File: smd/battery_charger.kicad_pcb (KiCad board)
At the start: 2 copper layers, 18.8 x 9.4 mm, 8 parts, among them J1 USB_OTG, U1 MCP73831

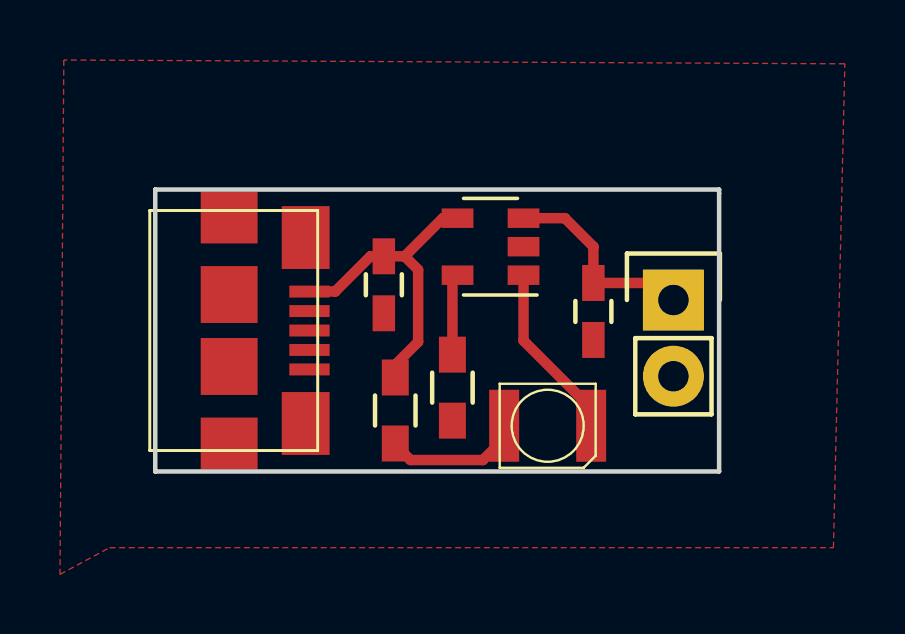
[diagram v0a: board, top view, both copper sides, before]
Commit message: Made the board almost half as big as before
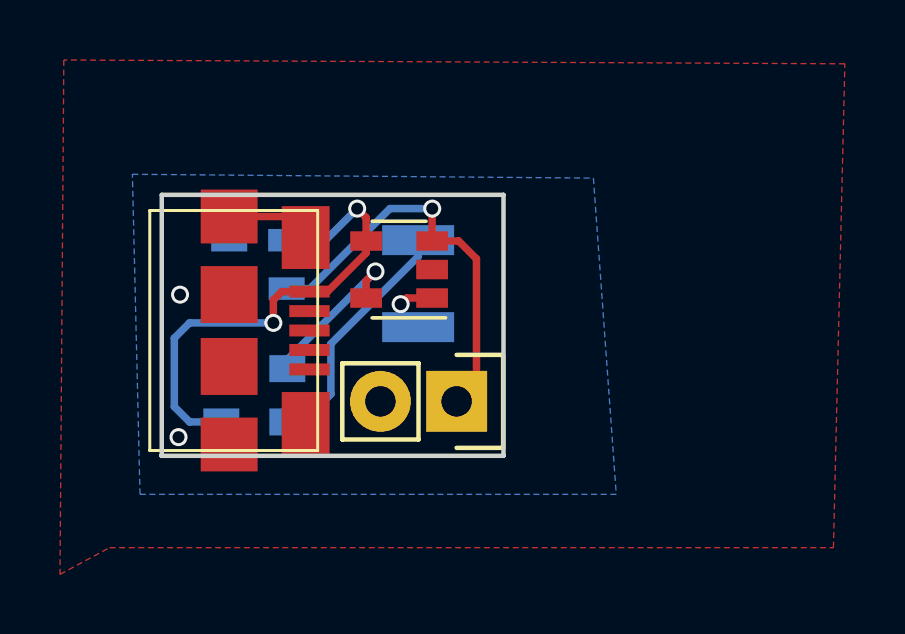
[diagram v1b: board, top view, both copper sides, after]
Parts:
- C1, C2, D1, R1, R2: moved to B.Cu
- moved C2 11.2 mm to (139.2, 104.0), turned to 180 degrees
- moved BT1 7.98 mm to (145.8, 107.7), turned to 180 degrees
- moved R2 6.63 mm to (139.1, 106.6), turned to 0 degrees
- moved D1 6.41 mm to (144.5, 103.8), turned to 180 degrees
- moved R1 4.71 mm to (139.1, 108.4), turned to 0 degrees
- moved C1 4.46 mm to (139.2, 102.3), turned to 0 degrees
- moved U1 3.14 mm to (143.9, 103.3)
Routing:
- net Net-(BT1-Pad1): track 6.83 -> 13.8 mm, vias 0 -> 1
- net +5V: track 10.4 -> 16.5 mm, vias 0 -> 2
- net Net-(D1-Pad1): track 5.95 -> 2.21 mm, vias 0 -> 1
- net Net-(D1-Pad2): track 4.61 -> 8.17 mm
- net GNDREF: track 0.00 -> 2.84 mm, vias 0 -> 2
- net Net-(R2-Pad2): track 2.72 -> 5.48 mm, vias 0 -> 1
- added copper zone on B.Cu, net GNDREF
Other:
- board size 18.8 x 9.4 mm -> 11.4 x 8.7 mm
- net class Default: trace_width 0.35 -> 0.25
- board text added: "github/elmameto"
- board text removed: "Plug and play single cell battery charger, based on the MCP73831 chip. Configured to deliver <500mA @ 4.2V. Layout designed by Matias Fernando Mamone github/elmameto"
